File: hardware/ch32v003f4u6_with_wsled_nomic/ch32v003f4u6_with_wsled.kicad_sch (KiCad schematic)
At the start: 23 parts, among them J2 PGM, J4 USB_C_Receptacle_USB2.0, J5 HOLE, J6 HOLE, U1 CH32V003F4U6, U2 3.3vReg

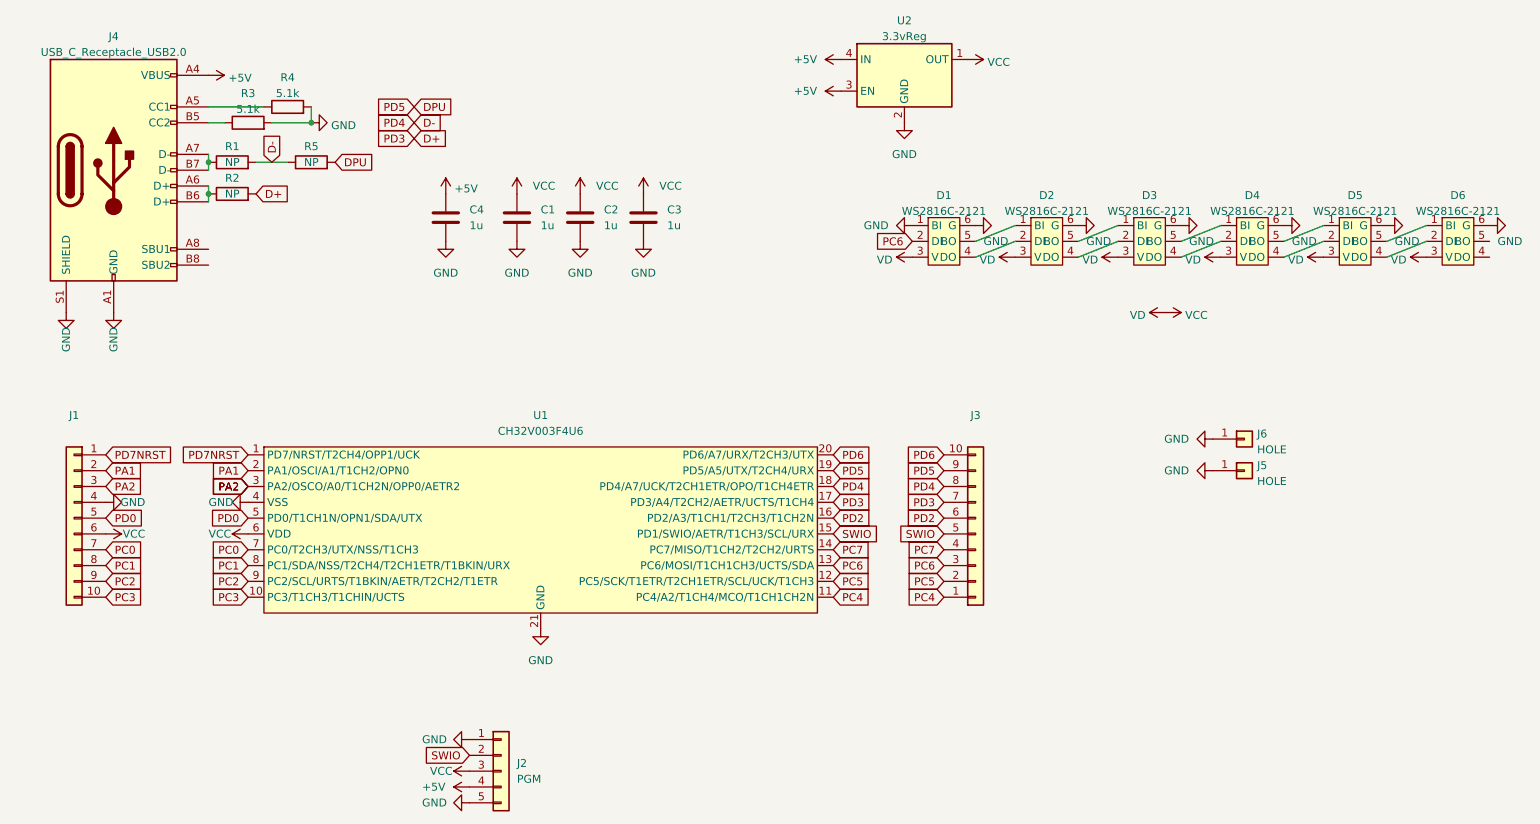
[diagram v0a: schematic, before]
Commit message: Switch over to using a .c file instead of a .S file for the startup code.  Helps make order-of-compiling not matter.
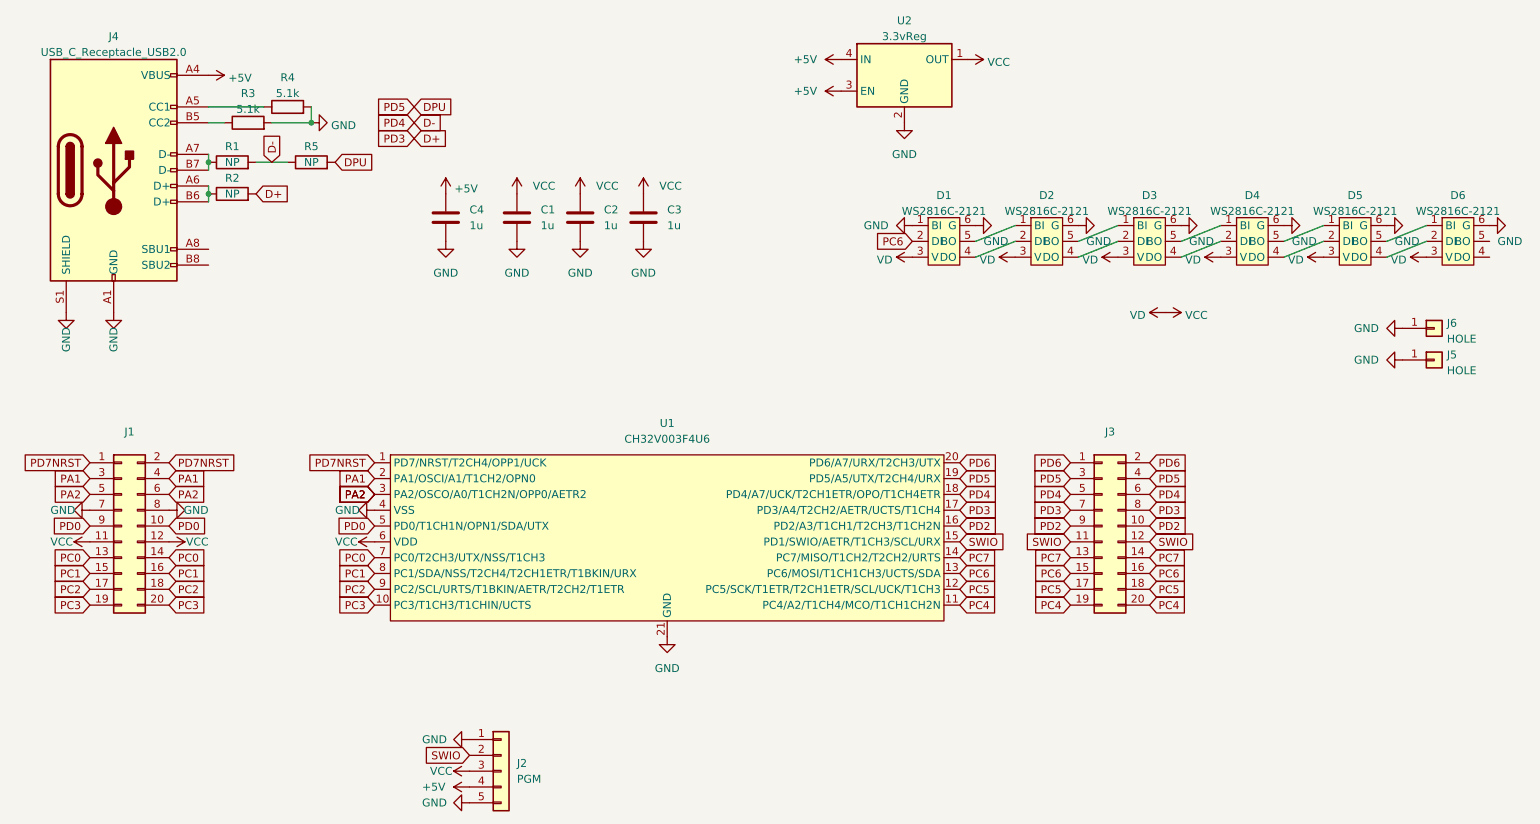
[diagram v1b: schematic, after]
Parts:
- removed J1, J3: ~, Connector_PinHeader_2.54mm:PinHeader_1x10_P2.54mm_Vertical, symbol Connector_Generic:Conn_01x10
- added J1, J3: ~, Connector_PinHeader_2.54mm:PinHeader_2x10_P2.54mm_Vertical, symbol Connector_Generic:Conn_02x10_Odd_Even
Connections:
- net D+: now also J3.7 (Pin_7), J3.8 (Pin_8)
- net D-: now also J3.5 (Pin_5), J3.6 (Pin_6)
- net DPU: now also J3.3 (Pin_3), J3.4 (Pin_4)
- net GND: now also J1.7 (Pin_7), J1.8 (Pin_8)
- net PA1: now also J1.3 (Pin_3), J1.4 (Pin_4)
- net PA2: now also J1.5 (Pin_5), J1.6 (Pin_6)
- net PC0: now also J1.13 (Pin_13), J1.14 (Pin_14)
- net PC1: now also J1.15 (Pin_15), J1.16 (Pin_16)
- net PC2: now also J1.17 (Pin_17), J1.18 (Pin_18)
- net PC3: now also J1.19 (Pin_19), J1.20 (Pin_20)
- net PC4: now also J3.19 (Pin_19), J3.20 (Pin_20)
- net PC5: now also J3.17 (Pin_17), J3.18 (Pin_18)
- net PC6: now also J3.15 (Pin_15), J3.16 (Pin_16)
- net PC7: now also J3.13 (Pin_13), J3.14 (Pin_14)
- net PD0: now also J1.10 (Pin_10), J1.9 (Pin_9)
- net PD2: now also J3.10 (Pin_10), J3.9 (Pin_9)
- net PD6: now also J3.1 (Pin_1), J3.2 (Pin_2)
- net PD7NRST: now also J1.1 (Pin_1), J1.2 (Pin_2)
- net SWIO: now also J3.11 (Pin_11), J3.12 (Pin_12)
- net VCC: now also J1.11 (Pin_11), J1.12 (Pin_12)
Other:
- moved on the sheet: J5, J6, U1
